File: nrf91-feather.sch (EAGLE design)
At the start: 93 parts, among them J2 CON-HEADER-1X12-MALE-PIN, J3 CON-HEADER-1X16-MALE-PIN, J4 CON-1909763-1, J5 CON-SIM-104224-0820, J6 CON-S2B-PH-SM4-TB(LF)(SN), J7 CON-1909763-1, J8 CON-USB-DX07S016JA1R1500, J9 CON-TC2030-MCP-NL, Q1 MOSFET-N-SC89, Q2 MOSFET-DUAL-COMP-SOT563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

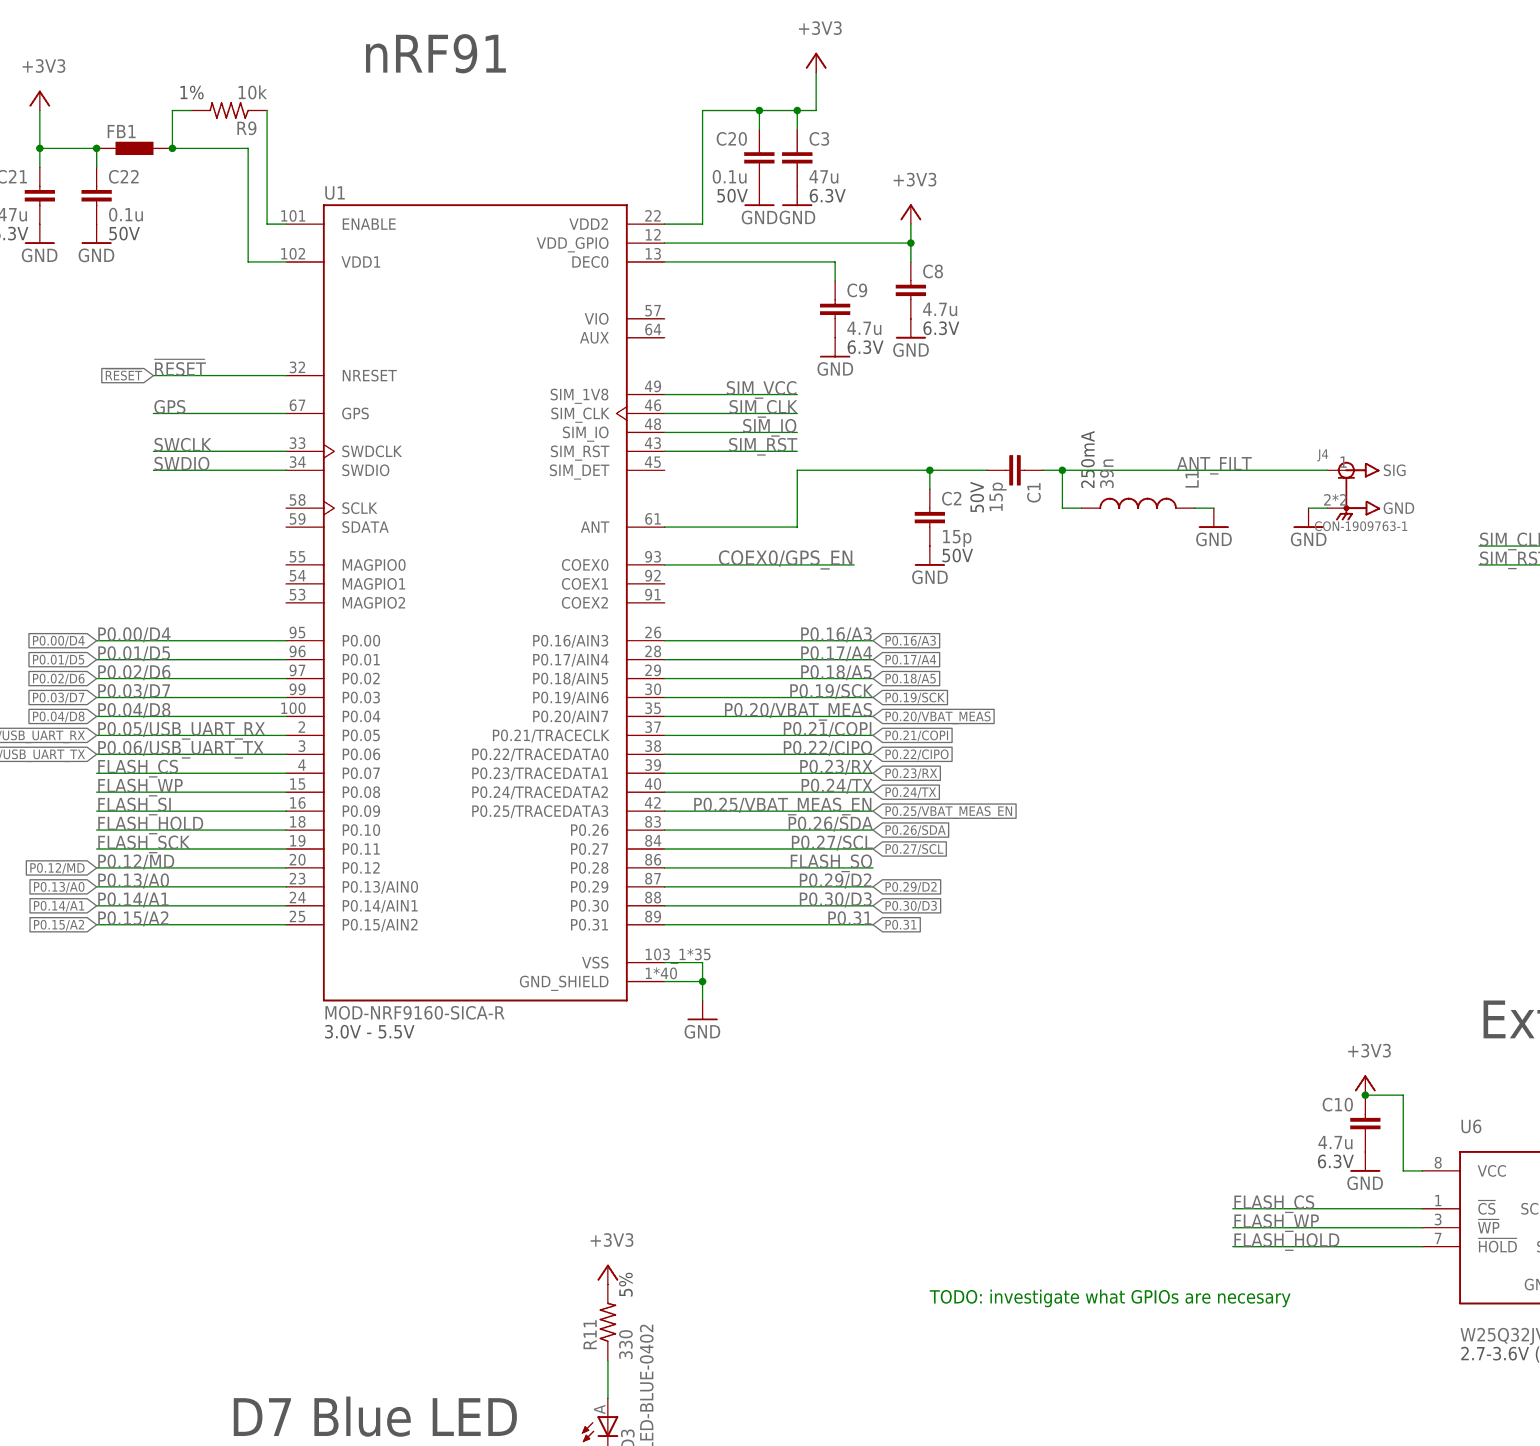
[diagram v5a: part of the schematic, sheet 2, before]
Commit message: Consolidating parts
Changed:
* R9 to 1k
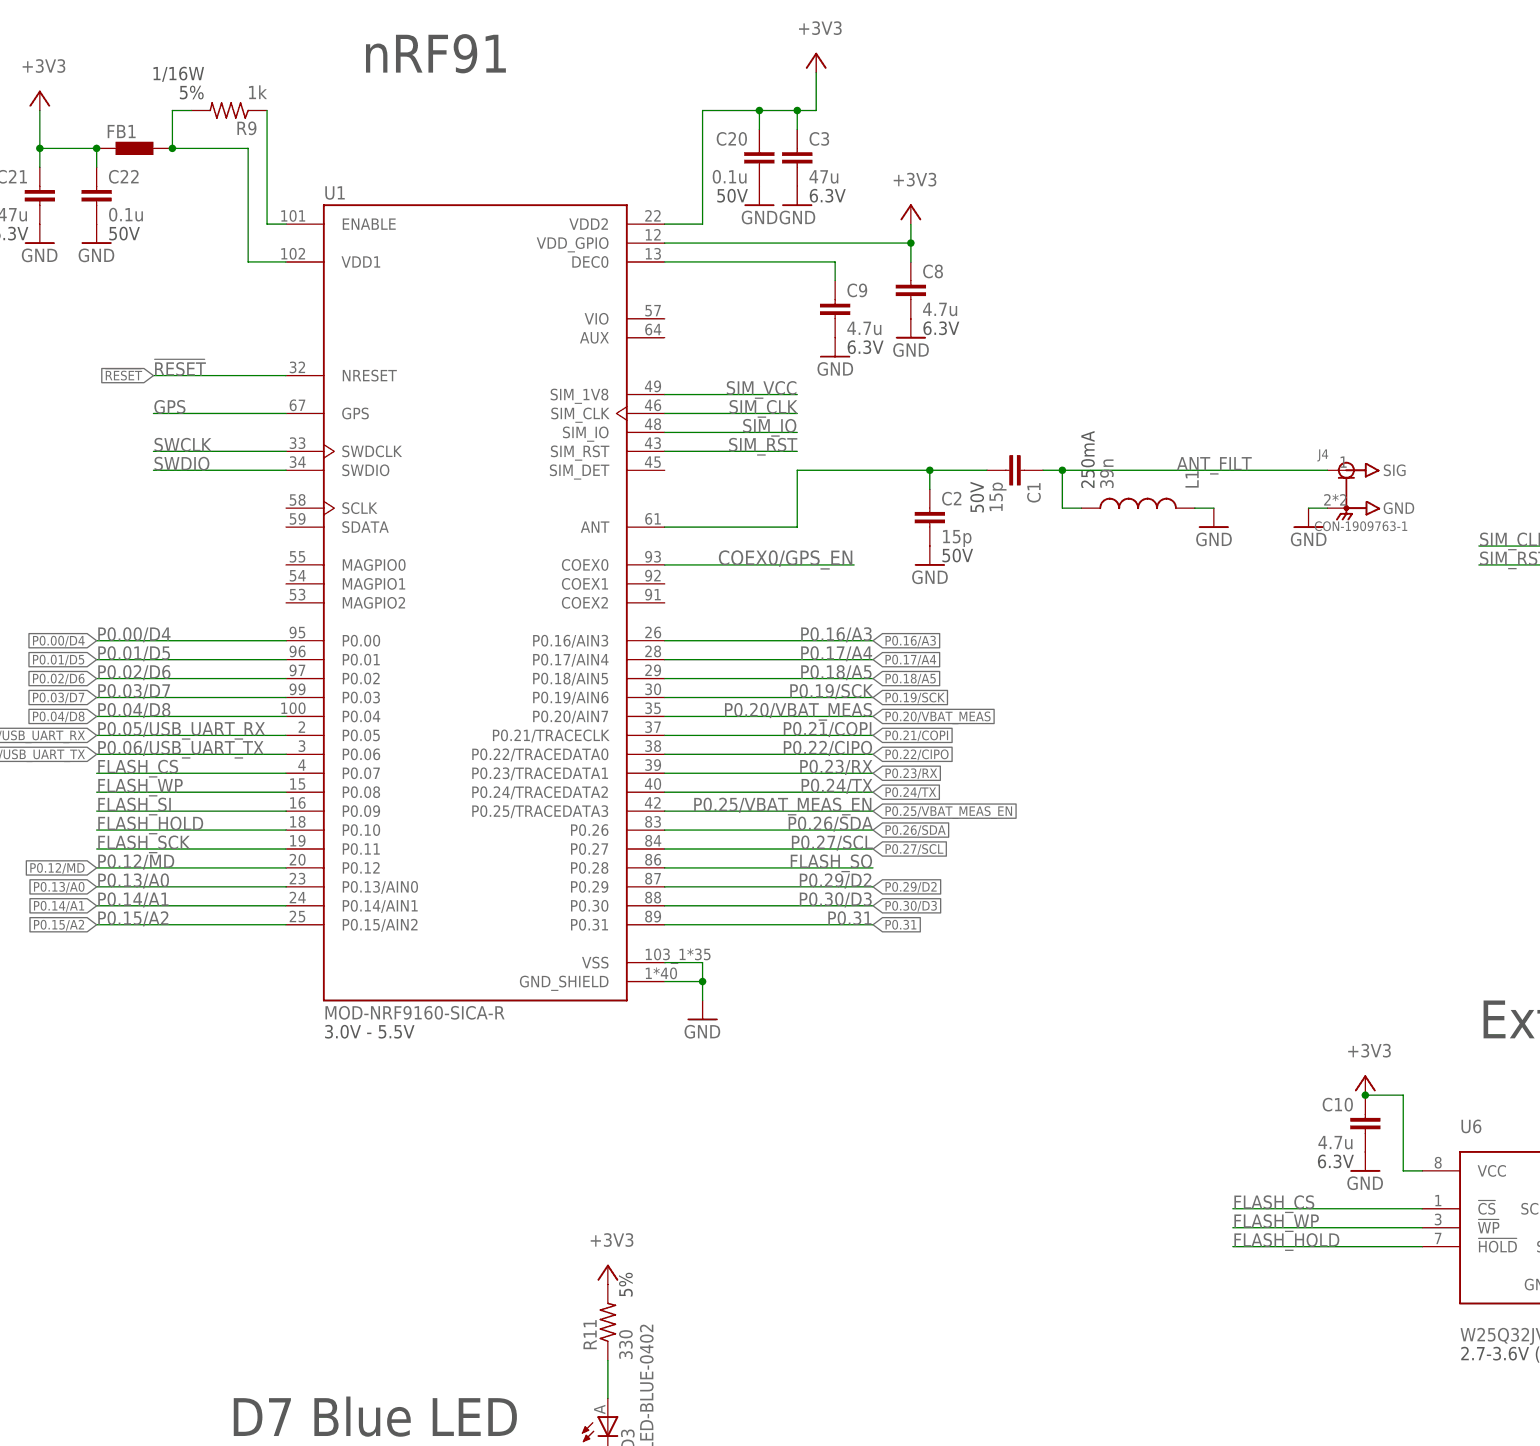
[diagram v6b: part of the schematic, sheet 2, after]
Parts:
- R9: value 10k -> 1k; device wolff-den:RES-10K-1%-0402 -> wolff-den:RES-1K-5%-0402
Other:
- note removed: "TODO: investigate what GPIOs are necesary"
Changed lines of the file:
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@@
 <part name="J5" library="wolff-den" library_urn="urn:adsk.eagle:library:6370453" deviceset="CON-SIM" device="" package3d_urn="urn:adsk.eagle:package:19415237/4" technology="-104224-0820"/>
 <part name="+3V3" library="supply1" library_urn="urn:adsk.eagle:library:371" deviceset="+3V3" device=""/>
-<part name="R9" library="wolff-den" library_urn="urn:adsk.eagle:library:6370453" deviceset="RES" device="-0402" package3d_urn="urn:adsk.eagle:package:19061974/5" technology="-10K-1%" value="10k"/>
+<part name="R9" library="wolff-den" library_urn="urn:adsk.eagle:library:6370453" deviceset="RES" device="-0402" package3d_urn="urn:adsk.eagle:package:19061974/5" technology="-1K-5%" value="1k"/>
 <part name="C8" library="wolff-den" library_urn="urn:adsk.eagle:library:6370453" deviceset="CAP" device="-0603" package3d_urn="urn:adsk.eagle:package:5807321/8" technology="-4.7U-6.3V-2" value="4.7u"/>
 <part name="GND12" library="supply1" library_urn="urn:adsk.eagle:library:371" deviceset="GND" device=""/>
@@
 <text x="134.62" y="15.24" size="3.81" layer="97">Some footprints provided by SnapEDA</text>
 <text x="134.62" y="10.16" size="3.81" layer="97">Some schematic symbols from Sparkfun</text>
-<text x="259.08" y="83.82" size="1.778" layer="91">TODO: investigate what GPIOs are necesary</text>
 </plain>
 <instances>

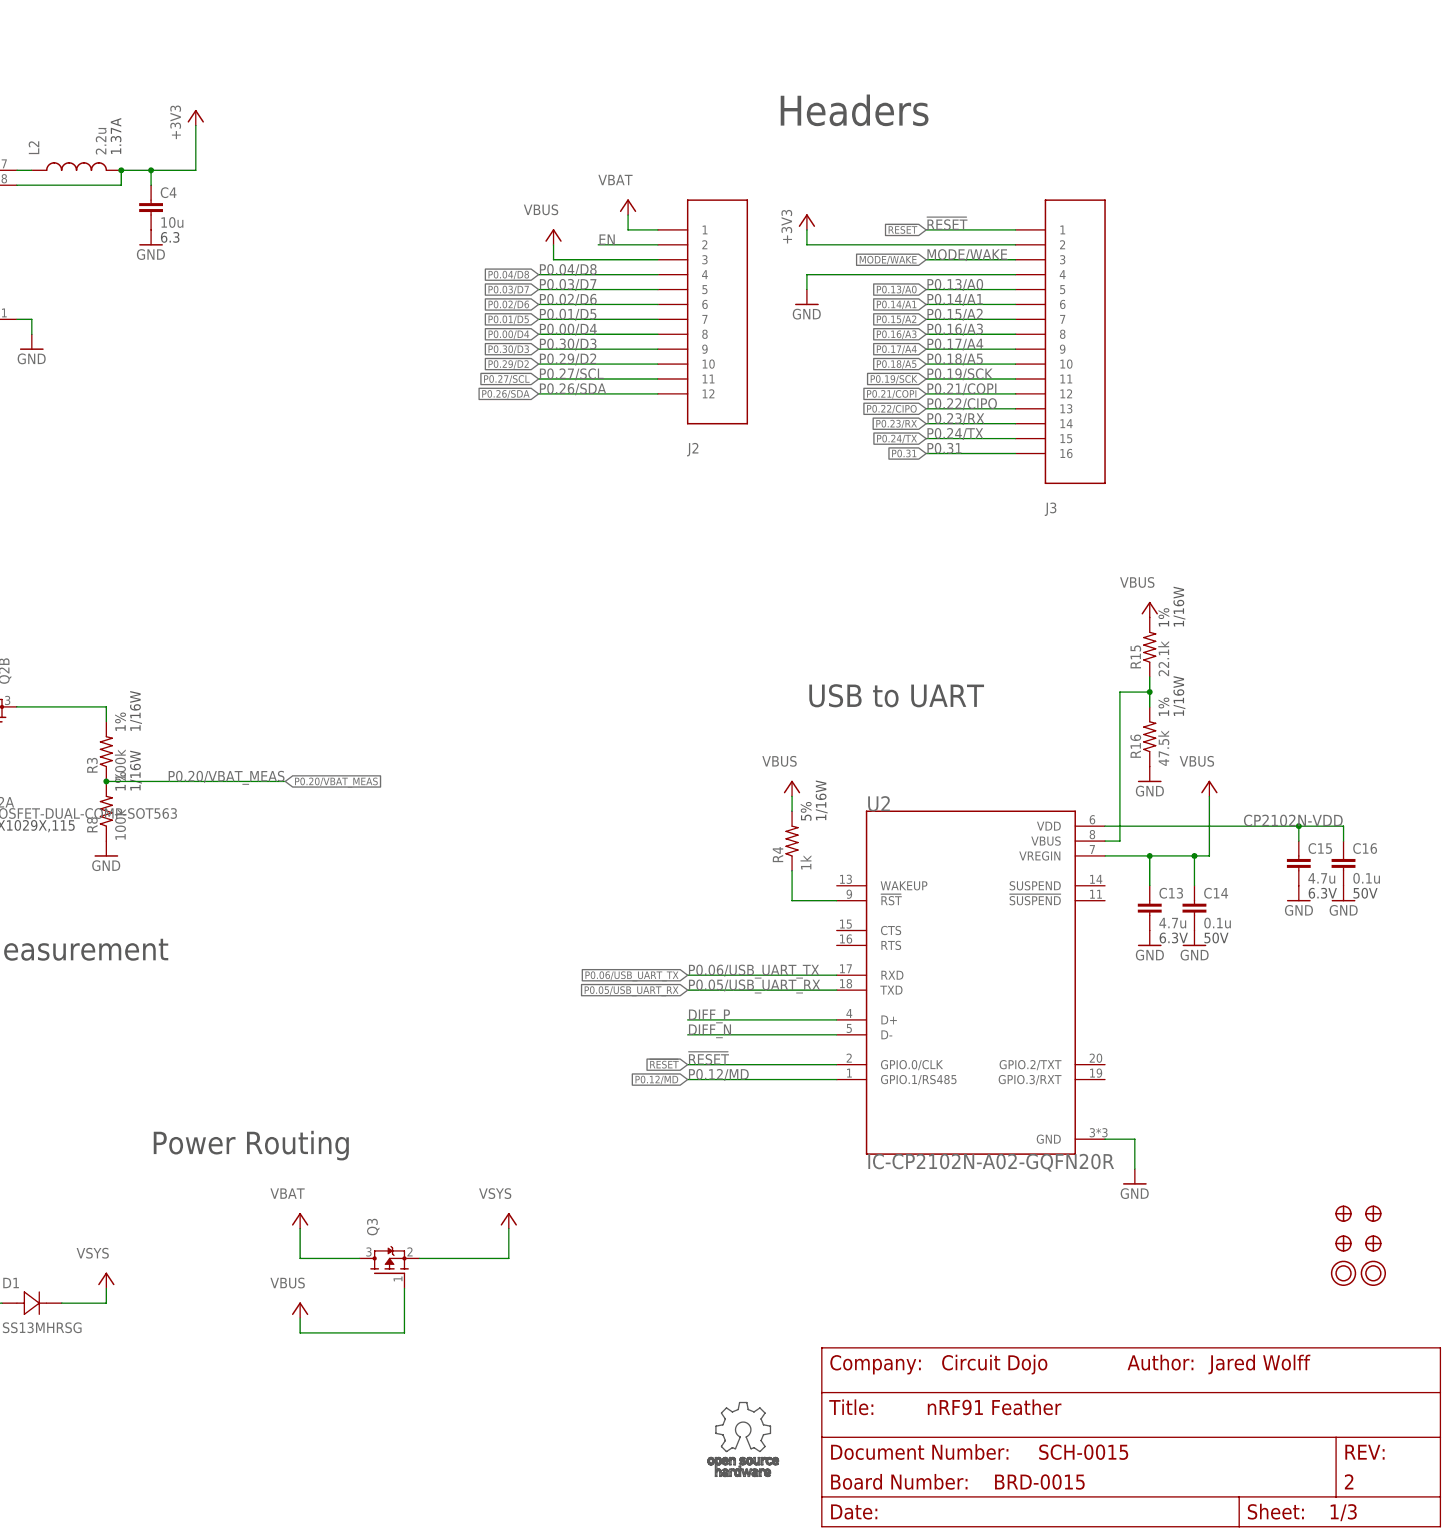
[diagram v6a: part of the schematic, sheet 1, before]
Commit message: Minor tweaks for production
Changed
* Fixed parts that don't have a tDocu reference designator
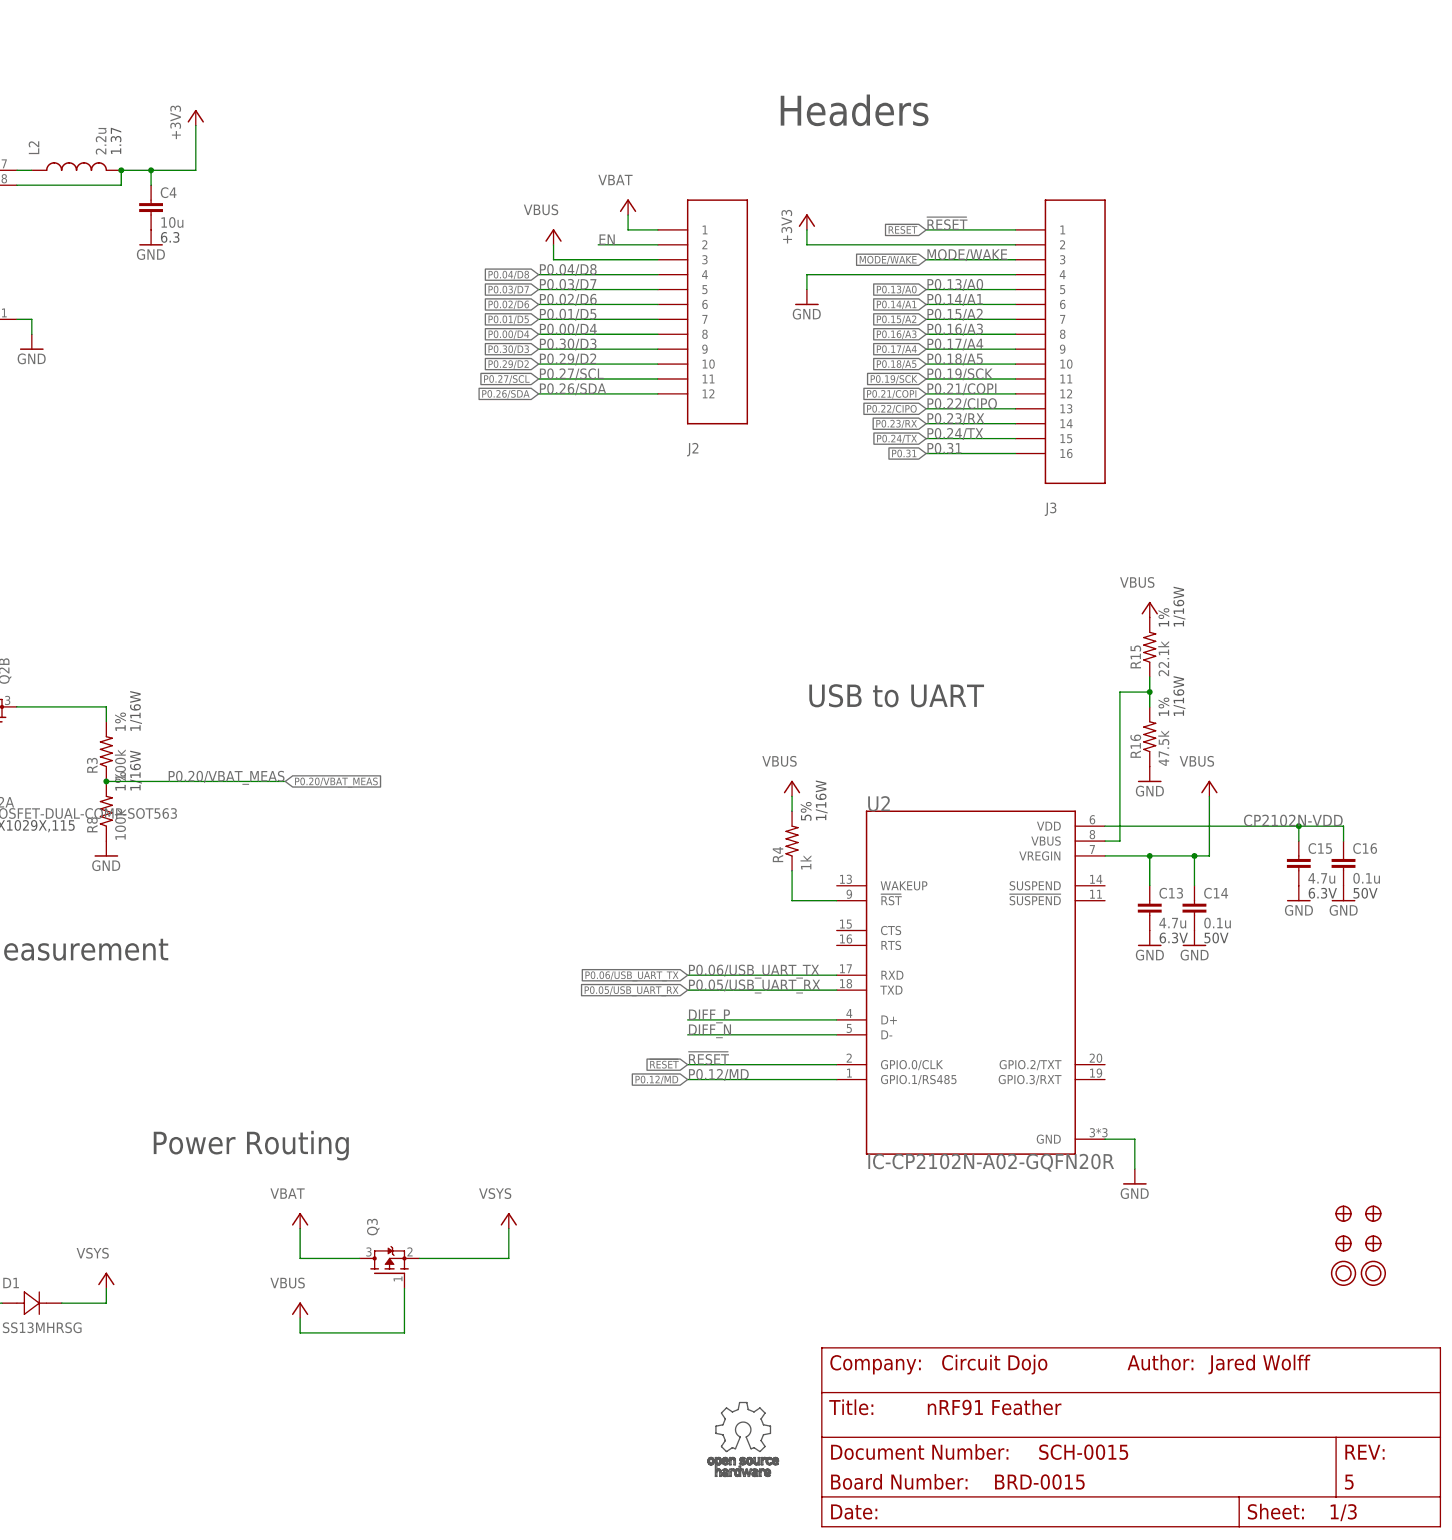
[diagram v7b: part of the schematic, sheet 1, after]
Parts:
- L2: device wolff-den:IND-0001 -> wolff-den:IND-2.2U-1.37A-2X2
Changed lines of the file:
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@@
 <attribute name="COMPANY" value="Circuit Dojo"/>
 <attribute name="DOC_NUMBER" value="SCH-0015"/>
-<attribute name="DOC_REV" value="2"/>
+<attribute name="DOC_REV" value="5"/>
 <attribute name="PN" value="PS-NRF91-FEATHER"/>
 <attribute name="TITLE" value="nRF91 Feather"/>
@@
 <part name="C4" library="wolff-den" library_urn="urn:adsk.eagle:library:6370453" deviceset="CAP" device="-0603" package3d_urn="urn:adsk.eagle:package:5807321/8" technology="-10U-6.3V" value="10u"/>
 <part name="P+3" library="wolff-den" library_urn="urn:adsk.eagle:library:6370453" deviceset="VBUS" device=""/>
-<part name="L2" library="wolff-den" library_urn="urn:adsk.eagle:library:6370453" deviceset="IND-0001" device="" package3d_urn="urn:adsk.eagle:package:5807324/5" value="2.2u"/>
+<part name="L2" library="wolff-den" library_urn="urn:adsk.eagle:library:6370453" deviceset="IND" device="" package3d_urn="urn:adsk.eagle:package:5807324/5" technology="-2.2U-1.37A-2X2" value="2.2u"/>
 <part name="P+7" library="wolff-den" library_urn="urn:adsk.eagle:library:6370453" deviceset="VSYS" device=""/>
 <part name="GND6" library="supply1" library_urn="urn:adsk.eagle:library:371" deviceset="GND" device=""/>
@@
 <part name="GND20" library="supply1" library_urn="urn:adsk.eagle:library:371" deviceset="GND" device=""/>
 <part name="GND28" library="supply1" library_urn="urn:adsk.eagle:library:371" deviceset="GND" device=""/>
-<part name="U5" library="wolff-den" library_urn="urn:adsk.eagle:library:6370453" deviceset="IC-BQ25170JDSGR" device="-WSON8" override_package3d_urn="urn:adsk.eagle:package:36693350/2" override_package_urn="urn:adsk.eagle:footprint:36693351/1"/>
+<part name="U5" library="wolff-den" library_urn="urn:adsk.eagle:library:6370453" deviceset="IC-BQ25170JDSGR" device="-WSON8" override_package3d_urn="urn:adsk.eagle:package:36693350/2" override_package_urn="urn:adsk.eagle:footprint:36693351/1" override_locally_modified="yes"/>
 <part name="GND42" library="supply1" library_urn="urn:adsk.eagle:library:371" deviceset="GND" device=""/>
 <part name="JMP2" library="wolff-den" library_urn="urn:adsk.eagle:library:6370453" deviceset="JUMPER-NO" device="-ROUND-NO" package3d_urn="urn:adsk.eagle:package:24898427/2"/>
